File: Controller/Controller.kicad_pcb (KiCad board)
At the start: 2 copper layers, 52 x 72 mm, 13 parts, among them J1 12Vin, J2 12V_underside, J3 Sensor_VCC_GND, J4 Sensor_1_2, J5 Sensor_3_4, J6 Relayboard, J7 RTC, J8 Buttons, U1 DOIT-ESP32-DEVKIT-V1

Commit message: changed PCB Layout
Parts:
- moved U1 2.84 mm to (154.9, 68.6)
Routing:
- net GND: track 62.2 -> 138.5 mm
- net +12V: track 0.00 -> 69.6 mm
- net +5V: track 25.3 -> 83.8 mm
- net Net-(J6-Pad5): track 0.00 -> 50.8 mm
- net Net-(J6-Pad4): track 0.00 -> 49.9 mm
- net Net-(J6-Pad3): track 0.00 -> 49.9 mm
- net Net-(J6-Pad2): track 0.00 -> 49.9 mm
- net Net-(J7-Pad5): track 0.00 -> 21.0 mm
- net Net-(J7-Pad4): track 0.00 -> 15.3 mm
- net Net-(J7-Pad1): track 0.00 -> 11.0 mm
- net Net-(J5-Pad1): track 18.7 -> 17.3 mm
- net Net-(J5-Pad2): track 17.6 -> 16.3 mm
- net Net-(J8-Pad5): track 8.35 -> 7.18 mm
- net Net-(J4-Pad2): track 19.8 -> 18.7 mm
- net Net-(J8-Pad4): track 8.35 -> 7.18 mm
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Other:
- board size 52 x 72 mm -> 55.9 x 77.2 mm

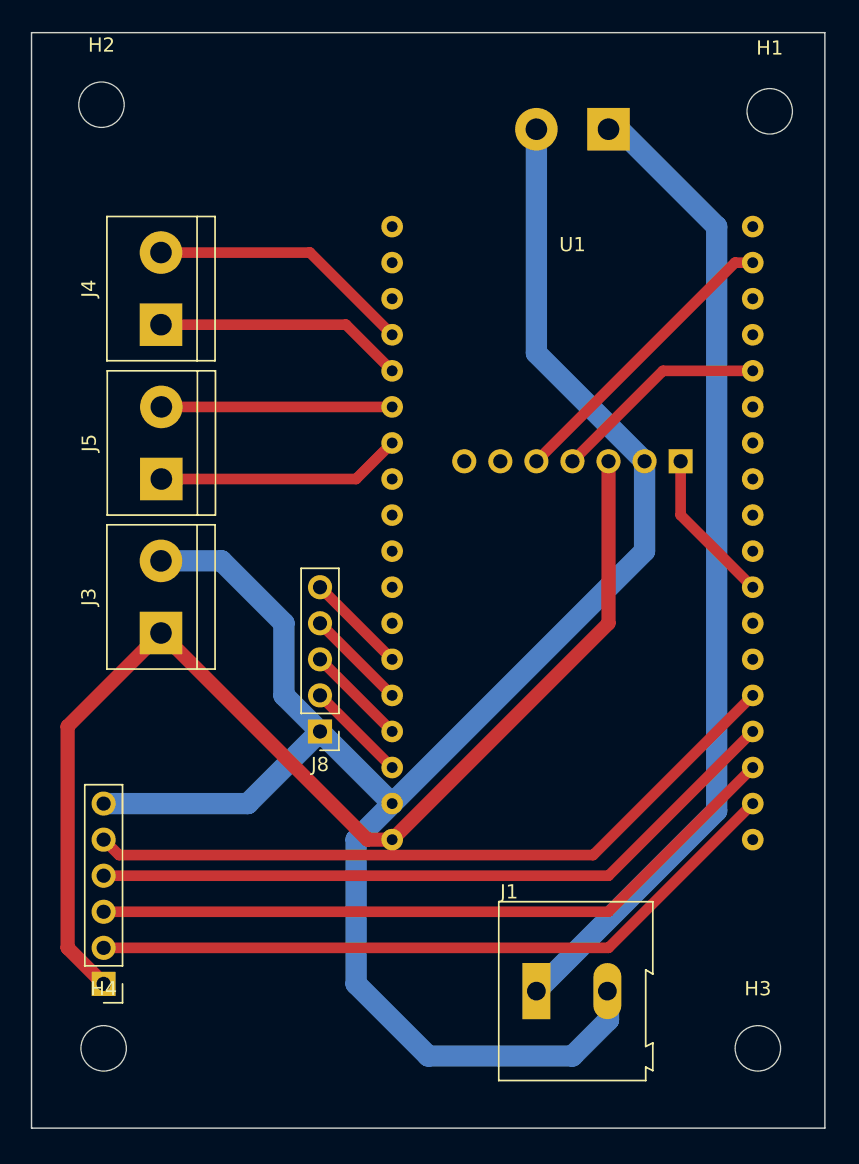
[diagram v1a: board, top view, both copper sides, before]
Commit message: switched 12V input pins for better routing
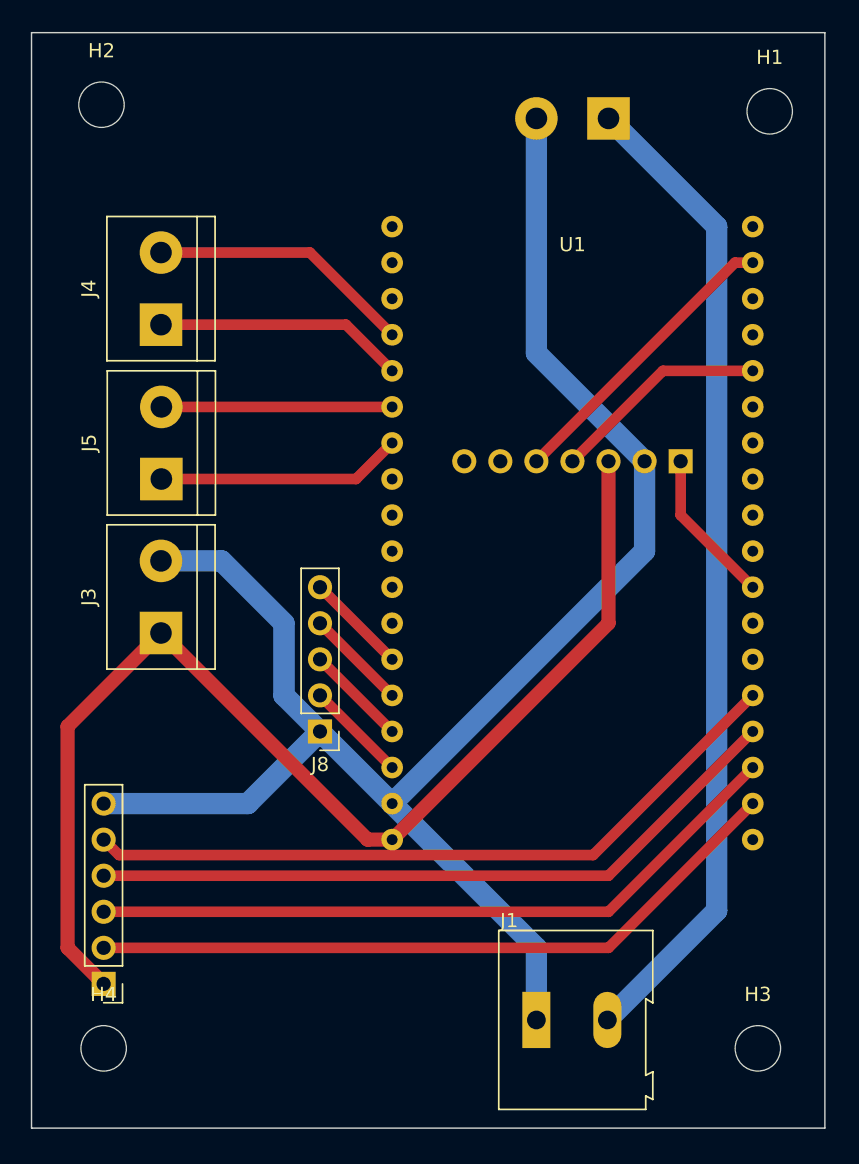
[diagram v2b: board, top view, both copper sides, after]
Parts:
- H1, H2, H3, H4: footprint MountingHole:MountingHole_3.2mm_M3 -> MountingHole:MountingHole_3.2mm_M3_DIN965
- moved J1 2.03 mm to (152.4, 127.0)
- moved J2 0.76 mm to (157.5, 63.5)
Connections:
- J1 pad 1: +12V -> GND
- J1 pad 2: GND -> +12V
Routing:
- net Net-(J6-Pad5): track 50.8 -> 0.00 mm
- net +5V: track 83.8 -> 134.6 mm
- net GND: track 138.5 -> 121.1 mm

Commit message: fix gnd connection
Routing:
- net GND: track 121.1 -> 121.9 mm
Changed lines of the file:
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@@
   (segment (start 132.08 111.76) (end 137.16 106.68) (width 1.5) (layer "B.Cu") (net 2))
   (segment (start 137.16 106.68) (end 134.62 104.14) (width 1.5) (layer "B.Cu") (net 2))
+  (segment (start 152.4 80.03) (end 152.4 63.5) (width 1.5) (layer "B.Cu") (net 2))
   (segment (start 152.4 80.03) (end 160.02 87.65) (width 1.5) (layer "B.Cu") (net 2))
   (segment (start 160.02 93.98) (end 160.02 87.65) (width 1.5) (layer "B.Cu") (net 2))
@@
   (segment (start 152.4 121.92) (end 152.4 127) (width 1.5) (layer "B.Cu") (net 2))
   (segment (start 134.62 104.14) (end 134.62 99.06) (width 1.5) (layer "B.Cu") (net 2))
-  (segment (start 152.4 64.262) (end 152.4 80.03) (width 1.5) (layer "B.Cu") (net 2))
   (segment (start 142.24 111.76) (end 152.4 121.92) (width 1.5) (layer "B.Cu") (net 2))
   (segment (start 134.62 99.06) (end 130.2258 94.6658) (width 1.5) (layer "B.Cu") (net 2))

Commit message: added Silkscreens, GND Polygons & more
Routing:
- net GND: track 121.9 -> 0.00 mm
- net Net-(J6-Pad5): track 0.00 -> 50.8 mm
- net +5V: track 134.6 -> 87.1 mm
- added copper zone on B.Cu, net GND
- added copper zone on F.Cu, net GND
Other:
- board text added: "12V"
- board text added: "2022"
- board text added: "5V"
- board text added: "Buttons"
- board text added: "Exellent1988"
- board text added: "GND"
- board text added: "RTC"
- board text added: "RelayBoard"
- board text added: "S1/2"
- board text added: "S3/4"
- board text added: "WaterController"
- board text added: "v1.0.0"
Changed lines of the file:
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@@
   )
   (paper "A4")
+  (title_block
+    (title "WaterController")
+    (date "2022-04-10")
+    (rev "v1.0.0")
+    (company "Exellent1988")
+  )
   (layers
     (0 "F.Cu" signal)
@@
     (property "Sheetname" "")
     (attr exclude_from_pos_files)
-    (fp_text reference "H4" (at 0 -3.8) (layer "F.SilkS")
+    (fp_text reference "H4" (at 4.2 0.16) (layer "F.SilkS")
       (effects (font (size 1 1) (thickness 0.15)))
     )
@@
     (property "Sheetname" "")
     (attr through_hole)
-    (fp_text reference "J4" (at 2.54 -5.08 90) (layer "F.SilkS")
+    (fp_text reference "J4" (at 2.54 5.1614 90) (layer "F.SilkS")
       (effects (font (size 1 1) (thickness 0.15)))
     )
@@
     (property "Sheetname" "")
     (attr through_hole)
-    (fp_text reference "J6" (at 0 -2.33) (layer "B.SilkS")
+    (fp_text reference "J6" (at -2.7 -0.2) (layer "B.SilkS")
       (effects (font (size 1 1) (thickness 0.15)) (justify mirror))
     )
@@
     (property "Sheetname" "")
     (attr through_hole)
-    (fp_text reference "J3" (at 2.54 -5.08 90) (layer "F.SilkS")
+    (fp_text reference "J3" (at 2.5858 5.1614 90) (layer "F.SilkS")
       (effects (font (size 1 1) (thickness 0.15)))
     )
@@
     (property "Sheetname" "")
     (attr through_hole)
-    (fp_text reference "J5" (at 2.54 -5.08 90) (layer "F.SilkS")
+    (fp_text reference "J5" (at 2.54 5.136 90) (layer "F.SilkS")
       (effects (font (size 1 1) (thickness 0.15)))
     )
@@
     (property "Sheetname" "")
     (attr through_hole)
-    (fp_text reference "J2" (at 2.54 5.08) (layer "B.SilkS")
+    (fp_text reference "J2" (at 2.54 -5.16) (layer "B.SilkS")
       (effects (font (size 1 1) (thickness 0.15)) (justify mirror))
     )
@@
   (gr_rect (start 168.44 124.79) (end 141.44 97.79) (layer "Eco1.User") (width 0.15) (fill none))
   (gr_rect (start 172.72 57.46) (end 116.84 134.62) (layer "Edge.Cuts") (width 0.1) (fill none))
+  (gr_text "GND" (at 163.12 85.16) (layer "B.SilkS")
+    (effects (font (size 1 1) (thickness 0.15)) (justify mirror))
+  )
+  (gr_text "12V" (at 162.12 63.66) (layer "B.SilkS")
+    (effects (font (size 1 1) (thickness 0.15)) (justify mirror))
+  )
+  (gr_text "RTC" (at 159.12 85.16) (layer "B.SilkS")
+    (effects (font (size 1 1) (thickness 0.15)) (justify mirror))
+  )
+  (gr_text "GND" (at 147.12 63.66) (layer "B.SilkS")
+    (effects (font (size 1 1) (thickness 0.15)) (justify mirror))
+  )
+  (gr_text "WaterController" (at 136.12 60.16) (layer "F.SilkS")
+    (effects (font (size 1.5 1.5) (thickness 0.3)))
+  )
+  (gr_text "GND" (at 119.62 94.66) (layer "F.SilkS")
+    (effects (font (size 1 1) (thickness 0.15)))
+  )
+  (gr_text "RelayBoard" (at 124.62 118.16 90) (layer "F.SilkS")
+    (effects (font (size 1 1) (thickness 0.15)))
+  )
+  (gr_text "S1/2" (at 119.62 75.66) (layer "F.SilkS")
+    (effects (font (size 1 1) (thickness 0.15)))
+  )
+  (gr_text "5V" (at 119.62 99.66) (layer "F.SilkS")
+    (effects (font (size 1 1) (thickness 0.15)))
+  )
+  (gr_text "12V" (at 162.62 127.16) (layer "F.SilkS")
+    (effects (font (size 1 1) (thickness 0.15)))
+  )
+  (gr_text "GND" (at 147.62 127.16) (layer "F.SilkS")
+    (effects (font (size 1 1) (thickness 0.15)))
+  )
+  (gr_text "S3/4" (at 119.62 86.16) (layer "F.SilkS")
+    (effects (font (size 1 1) (thickness 0.15)))
+  )
+  (gr_text "Buttons" (at 134.62 102.16 90) (layer "F.SilkS")
+    (effects (font (size 1 1) (thickness 0.15)))
+  )
+  (gr_text "2022" (at 132.62 131.66) (layer "F.SilkS")
+    (effects (font (size 1.5 1.5) (thickness 0.3)))
+  )
+  (gr_text "v1.0.0" (at 144.12 131.66) (layer "F.SilkS")
+    (effects (font (size 1.5 1.5) (thickness 0.3)))
+  )
+  (gr_text "Exellent1988" (at 134.62 62.66) (layer "F.SilkS")
+    (effects (font (size 1.5 1.5) (thickness 0.3)))
+  )
+  (gr_text "GND" (at 124.62 124.46 90) (layer "F.SilkS")
+    (effects (font (size 1 1) (thickness 0.15)))
+  )
+  (gr_text "GND" (at 134.62 107.16 90) (layer "F.SilkS")
+    (effects (font (size 1 1) (thickness 0.15)))
+  )
+  (dimension (type aligned) (layer "Eco1.User")
+    (pts (xy 116.84 57.46) (xy 172.72 57.46))
+    (height -3.8)
+    (gr_text "55,8800 mm" (at 144.78 52.51) (layer "Eco1.User")
+      (effects (font (size 1 1) (thickness 0.15)))
+    )
+    (format (units 3) (units_format 1) (precision 4))
+    (style (thickness 0.1) (arrow_length 1.27) (text_position_mode 0) (extension_height 0.58642) (extension_offset 0.5) keep_text_aligned)
+  )
+  (dimension (type aligned) (layer "Eco1.User")
+    (pts (xy 172.72 134.62) (xy 172.72 57.46))
+    (height 5.9)
+    (gr_text "77,1600 mm" (at 177.47 96.04 90) (layer "Eco1.User")
+      (effects (font (size 1 1) (thickness 0.15)))
+    )
+    (format (units 3) (units_format 1) (precision 4))
+    (style (thickness 0.1) (arrow_length 1.27) (text_position_mode 0) (extension_height 0.58642) (extension_offset 0.5) keep_text_aligned)
+  )
   (segment (start 165.1 119.3) (end 165.1 71.12) (width 1.5) (layer "B.Cu") (net 1))
   (segment (start 157.4 127) (end 165.1 119.3) (width 1.5) (layer "B.Cu") (net 1))
   (segment (start 165.1 71.12) (end 157.48 63.5) (width 1.5) (layer "B.Cu") (net 1))
-  (segment (start 121.92 111.76) (end 132.08 111.76) (width 1.5) (layer "B.Cu") (net 2))
-  (segment (start 132.08 111.76) (end 137.16 106.68) (width 1.5) (layer "B.Cu") (net 2))
-  (segment (start 137.16 106.68) (end 134.62 104.14) (width 1.5) (layer "B.Cu") (net 2))
-  (segment (start 152.4 80.03) (end 152.4 63.5) (width 1.5) (layer "B.Cu") (net 2))
-  (segment (start 152.4 80.03) (end 160.02 87.65) (width 1.5) (layer "B.Cu") (net 2))
-  (segment (start 160.02 93.98) (end 160.02 87.65) (width 1.5) (layer "B.Cu") (net 2))
-  (segment (start 130.2258 94.6658) (end 125.9586 94.6658) (width 1.5) (layer "B.Cu") (net 2))
-  (segment (start 142.24 111.76) (end 160.02 93.98) (width 1.5) (layer "B.Cu") (net 2))
-  (segment (start 152.4 121.92) (end 152.4 127) (width 1.5) (layer "B.Cu") (net 2))
-  (segment (start 134.62 104.14) (end 134.62 99.06) (width 1.5) (layer "B.Cu") (net 2))
-  (segment (start 142.24 111.76) (end 152.4 121.92) (width 1.5) (layer "B.Cu") (net 2))
-  (segment (start 134.62 99.06) (end 130.2258 94.6658) (width 1.5) (layer "B.Cu") (net 2))
-  (segment (start 137.16 106.68) (end 142.24 111.76) (width 1.5) (layer "B.Cu") (net 2))
+  (segment (start 147.98 114.3) (end 157.48 104.8) (width 1) (layer "F.Cu") (net 3))
   (segment (start 119.38 106.3244) (end 119.38 121.92) (width 1) (layer "F.Cu") (net 3))
-  (segment (start 157.48 87.65) (end 157.48 99.06) (width 1) (layer "F.Cu") (net 3))
-  (segment (start 157.48 99.06) (end 142.24 114.3) (width 1) (layer "F.Cu") (net 3))
-  (segment (start 121.92 114.3) (end 123.006511 115.386511) (width 0.75) (layer "F.Cu") (net 3))
   (segment (start 125.9586 99.7458) (end 119.38 106.3244) (width 1) (layer "F.Cu") (net 3))
-  (segment (start 156.393489 115.386511) (end 167.64 104.14) (width 0.75) (layer "F.Cu") (net 3))
+  (segment (start 157.48 104.8) (end 157.48 87.65) (width 1) (layer "F.Cu") (net 3))
   (segment (start 140.5128 114.3) (end 142.24 114.3) (width 1) (layer "F.Cu") (net 3))
   (segment (start 125.9586 99.7458) (end 140.5128 114.3) (width 1) (layer "F.Cu") (net 3))
+  (segment (start 142.24 114.3) (end 147.98 114.3) (width 1) (layer "F.Cu") (net 3))
   (segment (start 119.38 121.92) (end 121.92 124.46) (width 1) (layer "F.Cu") (net 3))
-  (segment (start 123.006511 115.386511) (end 156.393489 115.386511) (width 0.75) (layer "F.Cu") (net 3))
   (segment (start 125.9586 78.0288) (end 138.9888 78.0288) (width 0.75) (layer "F.Cu") (net 4))
   (segment (start 138.9888 78.0288) (end 142.24 81.28) (width 0.75) (layer "F.Cu") (net 4))
@@
   (segment (start 121.92 116.84) (end 157.48 116.84) (width 0.75) (layer "F.Cu") (net 12))
   (segment (start 157.48 116.84) (end 167.64 106.68) (width 0.75) (layer "F.Cu") (net 12))
+  (segment (start 121.92 114.3) (end 123.006511 115.386511) (width 0.75) (layer "F.Cu") (net 13))
+  (segment (start 156.393489 115.386511) (end 167.64 104.14) (width 0.75) (layer "F.Cu") (net 13))
+  (segment (start 123.006511 115.386511) (end 156.393489 115.386511) (width 0.75) (layer "F.Cu") (net 13))
   (segment (start 162.56 87.65) (end 162.56 91.44) (width 0.75) (layer "F.Cu") (net 14))
   (segment (start 162.56 91.44) (end 167.64 96.52) (width 0.75) (layer "F.Cu") (net 14))
@@
   (segment (start 142.24 104.14) (end 137.16 99.06) (width 0.75) (layer "F.Cu") (net 19))
   (segment (start 142.24 101.6) (end 137.16 96.52) (width 0.75) (layer "F.Cu") (net 20))
+  (zone (net 2) (net_name "GND") (layer "F.Cu") (hatch edge 0.508)
+    (connect_pads (clearance 0.508))
+    (min_thickness 0.254) (filled_areas_thickness no)
+    (fill yes (thermal_gap 0.508) (thermal_bridge_width 0.508))
+    (polygon
+      (pts
+        (xy 173.12 135.16)
+        (xy 116.62 135.16)
+        (xy 116.62 57.16)
+        (xy 173.12 57.16)
+      )
+    )
+  )
+  (zone (net 2) (net_name "GND") (layer "B.Cu") (hatch edge 0.508)
+    (connect_pads (clearance 0.508))
+    (min_thickness 0.254) (filled_areas_thickness no)
+    (fill yes (thermal_gap 0.508) (thermal_bridge_width 0.508))
+    (polygon
+      (pts
+        (xy 173.12 135.16)
+        (xy 116.62 135.16)
+        (xy 116.62 57.16)
+        (xy 173.12 57.16)
+      )
+    )
+  )
   (group "" (id 9f433da6-bc26-4475-8b29-5cf7a8fdea20)
     (members

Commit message: fixed some layout stuff -pcb
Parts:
- U1 - DOIT ESP32 V1 36Pin : renamed from U1
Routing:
- net Net-(J6-Pad4): track 49.9 -> 52.0 mm
- net Net-(J6-Pad3): track 49.9 -> 51.2 mm
- net Net-(J6-Pad5): track 50.8 -> 52.0 mm
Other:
- board text added: "@Exellent1988"
- board text removed: "Exellent1988"
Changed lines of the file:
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@@
     (property "Sheetname" "")
     (attr through_hole)
-    (fp_text reference "U1" (at 0 3.81) (layer "F.SilkS")
+    (fp_text reference "U1 - DOIT ESP32 V1 36Pin " (at 0.254 32.004 90) (layer "F.SilkS")
       (effects (font (size 1 1) (thickness 0.15)))
     )
@@
     )
   )
+  (gr_rect (start 168.62 124.66) (end 141.62 97.66) (layer "B.SilkS") (width 0.15) (fill none))
+  (gr_rect (start 140.92 69.76) (end 168.82 116.76) (layer "F.SilkS") (width 0.15) (fill none))
   (gr_rect (start 168.44 124.79) (end 141.44 97.79) (layer "Eco1.User") (width 0.15) (fill none))
   (gr_rect (start 172.72 57.46) (end 116.84 134.62) (layer "Edge.Cuts") (width 0.1) (fill none))
-  (gr_text "GND" (at 163.12 85.16) (layer "B.SilkS")
-    (effects (font (size 1 1) (thickness 0.15)) (justify mirror))
-  )
   (gr_text "12V" (at 162.12 63.66) (layer "B.SilkS")
     (effects (font (size 1 1) (thickness 0.15)) (justify mirror))
   )
-  (gr_text "RTC" (at 159.12 85.16) (layer "B.SilkS")
+  (gr_text "RTC" (at 154.94 106.68) (layer "B.SilkS")
     (effects (font (size 1 1) (thickness 0.15)) (justify mirror))
   )
@@
     (effects (font (size 1.5 1.5) (thickness 0.3)))
   )
-  (gr_text "Exellent1988" (at 134.62 62.66) (layer "F.SilkS")
-    (effects (font (size 1.5 1.5) (thickness 0.3)))
-  )
-  (gr_text "GND" (at 124.62 124.46 90) (layer "F.SilkS")
+  (gr_text "@Exellent1988" (at 135.62 62.76) (layer "F.SilkS")
+    (effects (font (size 1.5 1.5) (thickness 0.3) italic))
+  )
+  (gr_text "5V" (at 124.62 124.66 90) (layer "F.SilkS")
+    (effects (font (size 1 1) (thickness 0.15)))
+  )
+  (gr_text "GND" (at 124.72 111.56 90) (layer "F.SilkS")
     (effects (font (size 1 1) (thickness 0.15)))
   )
@@
     (pts (xy 116.84 57.46) (xy 172.72 57.46))
     (height -3.8)
-    (gr_text "55,8800 mm" (at 144.78 52.51) (layer "Eco1.User")
+    (gr_text "55.8800 mm" (at 144.78 52.51) (layer "Eco1.User")
       (effects (font (size 1 1) (thickness 0.15)))
     )
@@
     (pts (xy 172.72 134.62) (xy 172.72 57.46))
     (height 5.9)
-    (gr_text "77,1600 mm" (at 177.47 96.04 90) (layer "Eco1.User")
+    (gr_text "77.1600 mm" (at 177.47 96.04 90) (layer "Eco1.User")
       (effects (font (size 1 1) (thickness 0.15)))
     )
@@
   (segment (start 121.92 121.92) (end 157.48 121.92) (width 0.75) (layer "F.Cu") (net 10))
   (segment (start 157.48 121.92) (end 167.64 111.76) (width 0.75) (layer "F.Cu") (net 10))
-  (segment (start 157.48 119.38) (end 167.64 109.22) (width 0.75) (layer "F.Cu") (net 11))
-  (segment (start 121.92 119.38) (end 157.48 119.38) (width 0.75) (layer "F.Cu") (net 11))
-  (segment (start 121.92 116.84) (end 157.48 116.84) (width 0.75) (layer "F.Cu") (net 12))
-  (segment (start 157.48 116.84) (end 167.64 106.68) (width 0.75) (layer "F.Cu") (net 12))
-  (segment (start 121.92 114.3) (end 123.006511 115.386511) (width 0.75) (layer "F.Cu") (net 13))
-  (segment (start 156.393489 115.386511) (end 167.64 104.14) (width 0.75) (layer "F.Cu") (net 13))
-  (segment (start 123.006511 115.386511) (end 156.393489 115.386511) (width 0.75) (layer "F.Cu") (net 13))
+  (segment (start 155.88952 120.97048) (end 167.64 109.22) (width 0.75) (layer "F.Cu") (net 11))
+  (segment (start 121.92 119.38) (end 123.51048 120.97048) (width 0.75) (layer "F.Cu") (net 11))
+  (segment (start 123.51048 120.97048) (end 155.88952 120.97048) (width 0.75) (layer "F.Cu") (net 11))
+  (segment (start 121.92 116.84) (end 124.46 119.38) (width 0.75) (layer "F.Cu") (net 12))
+  (segment (start 154.94 119.38) (end 167.64 106.68) (width 0.75) (layer "F.Cu") (net 12))
+  (segment (start 124.46 119.38) (end 154.94 119.38) (width 0.75) (layer "F.Cu") (net 12))
+  (segment (start 154.94 116.84) (end 167.64 104.14) (width 0.75) (layer "F.Cu") (net 13))
+  (segment (start 121.92 114.3) (end 124.46 116.84) (width 0.75) (layer "F.Cu") (net 13))
+  (segment (start 124.46 116.84) (end 154.94 116.84) (width 0.75) (layer "F.Cu") (net 13))
   (segment (start 162.56 87.65) (end 162.56 91.44) (width 0.75) (layer "F.Cu") (net 14))
   (segment (start 162.56 91.44) (end 167.64 96.52) (width 0.75) (layer "F.Cu") (net 14))
